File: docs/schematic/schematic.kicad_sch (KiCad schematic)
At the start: 9 parts, among them J1 AudioJack2, SW1 SW_Push, SW2 SW_Push, SW3 SW_Push, SW4 SW_Push

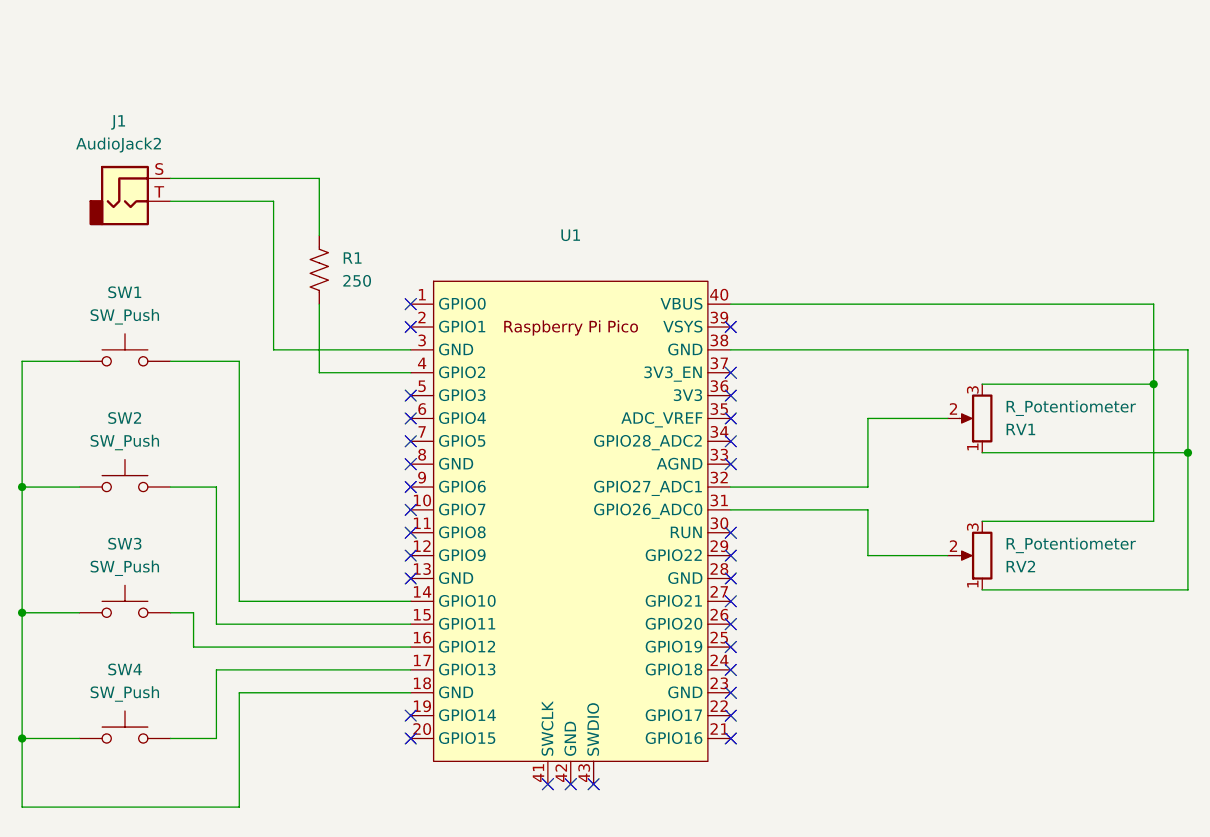
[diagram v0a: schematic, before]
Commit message: Update Schematic to as built
We deviated from the original schematic as it was simpler to construct/ source in the way we built  it.
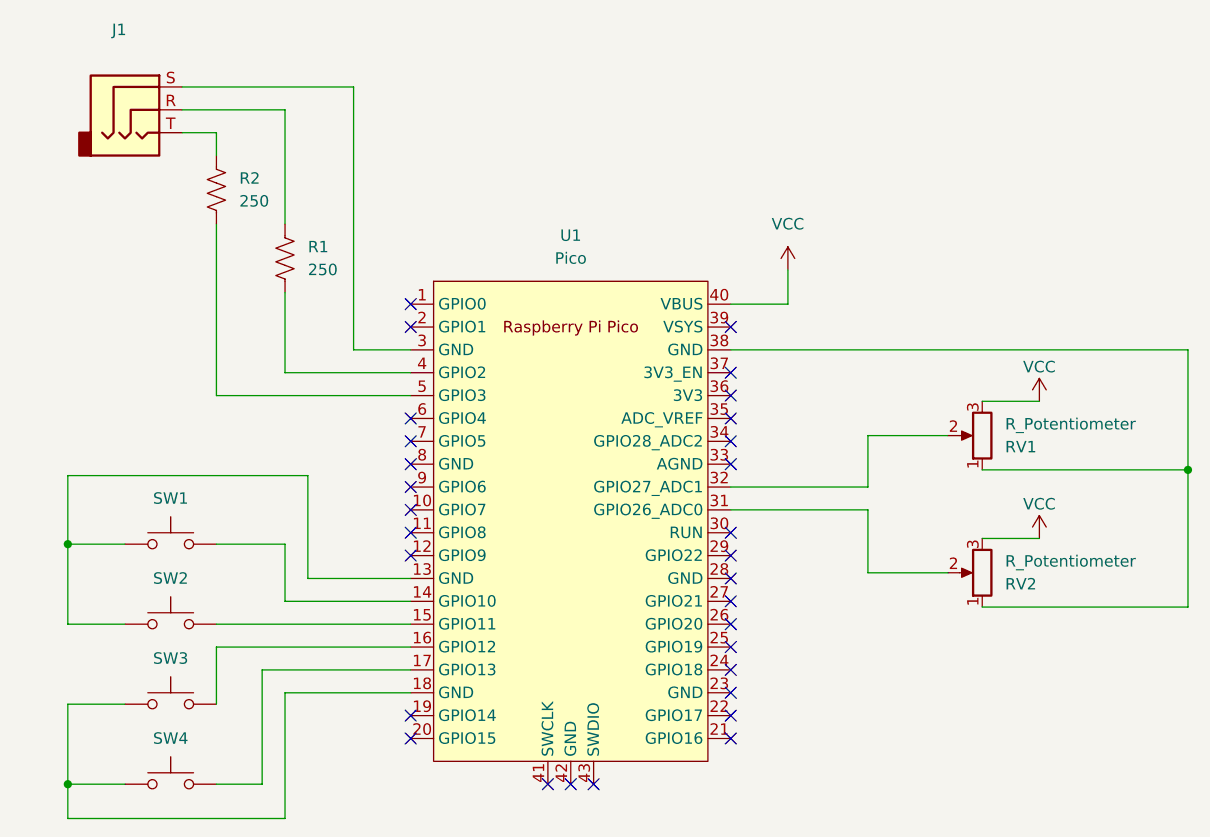
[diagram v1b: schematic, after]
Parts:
- removed J1: AudioJack2, Connector_Wire:SolderWire-0.15sqmm_1x02_P4mm_D0.5mm_OD1.5mm, symbol Connector:AudioJack2
- added J1: (no value), symbol Connector:AudioJack3
- added R2: 250, Resistor_THT:R_Axial_DIN0309_L9.0mm_D3.2mm_P15.24mm_Horizontal, symbol Device:R_US
- U1: value (none) -> Pico; footprint (none) -> MCU_RaspberryPi_and_Boards:RPi_Pico_SMD_TH
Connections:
- net at SW3.1, SW4.1, U1.18 (GND): no longer SW1.1, SW2.1
- net at R1.1: now also J1.R
- net VCC: now reaches RV1.3, RV2.3, U1.40 (VBUS)
- net at U1.3 (GND): now also J1.S
- net at U1.13 (GND): now also SW1.1, SW2.1
- net at U1.5 (GPIO3): now also R2.2
- new net: J1.T, R2.1
- no-connect marks 32 -> 30
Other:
- moved on the sheet: R1, RV1, RV2, SW2, SW3, SW4

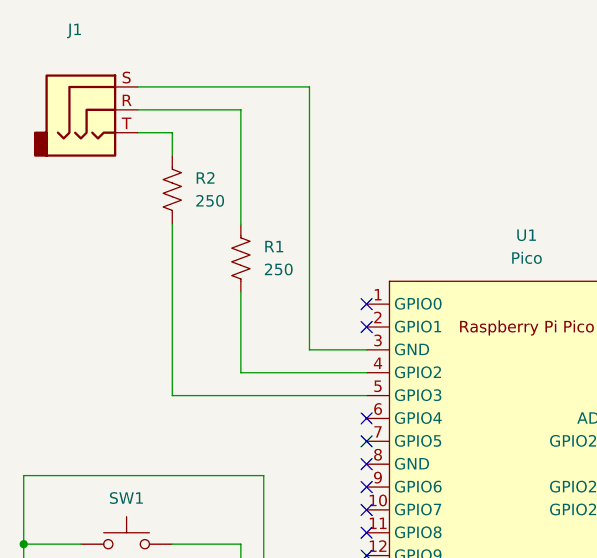
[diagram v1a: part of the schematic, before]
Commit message: Update Schematic
We found that the tone() function can only service one pin at a time, and that we can tie the t and r of the audio output together with no ill effects.
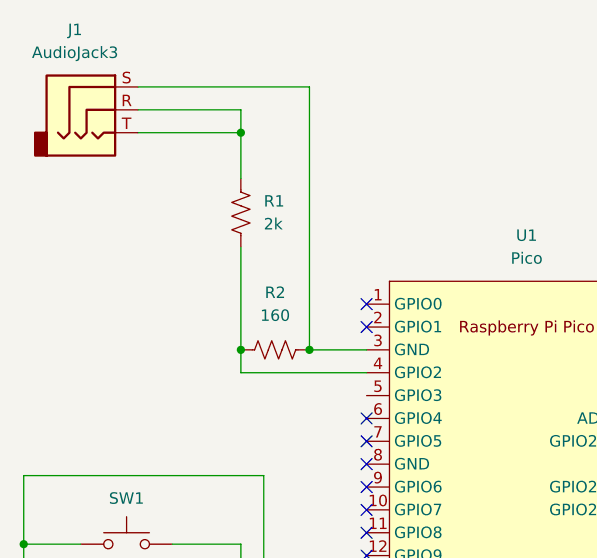
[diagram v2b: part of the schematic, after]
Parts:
- J1: value (none) -> AudioJack3; footprint (none) -> Connector_Audio:Jack_6.35mm_Neutrik_NJ3FD-V_Vertical
- R1: value 250 -> 2k
- R2: value 250 -> 160
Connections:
- net at J1.T: now also J1.R, R1.1; no longer R2.1
- net at R2.2: now also J1.S, U1.3 (GND); no longer U1.5 (GPIO3)
- net at R1.2, U1.4 (GPIO2): now also R2.1
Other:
- moved on the sheet: R1
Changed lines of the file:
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@@
     (rev "1.1")
   )
+  (junction (at 88.9 43.18) (diameter 0) (color 0 0 0 0)
+  )
   (junction (at 64.77 115.57) (diameter 0) (color 0 0 0 0)
+  )
+  (junction (at 96.52 67.31) (diameter 0) (color 0 0 0 0)
+  )
+  (junction (at 88.9 67.31) (diameter 0) (color 0 0 0 0)
   )
   (junction (at 189.23 80.645) (diameter 0) (color 0 0 0 0)
@@
     (stroke (width 0) (type default) (color 0 0 0 0))
   )
-  (wire (pts (xy 77.47 43.18) (xy 81.28 43.18))
-    (stroke (width 0) (type default) (color 0 0 0 0))
-  )
   (wire (pts (xy 88.9 95.25) (xy 102.87 95.25))
     (stroke (width 0) (type default) (color 0 0 0 0))
   )
+  (wire (pts (xy 88.9 67.31) (xy 88.9 69.85))
+    (stroke (width 0) (type default) (color 0 0 0 0))
+  )
   (wire (pts (xy 91.44 81.28) (xy 64.77 81.28))
     (stroke (width 0) (type default) (color 0 0 0 0))
@@
     (stroke (width 0) (type default) (color 0 0 0 0))
   )
-  (wire (pts (xy 81.28 43.18) (xy 81.28 45.72))
-    (stroke (width 0) (type default) (color 0 0 0 0))
-  )
   (wire (pts (xy 138.43 62.23) (xy 144.78 62.23))
     (stroke (width 0) (type default) (color 0 0 0 0))
@@
     (stroke (width 0) (type default) (color 0 0 0 0))
   )
-  (wire (pts (xy 96.52 67.31) (xy 96.52 38.1))
-    (stroke (width 0) (type default) (color 0 0 0 0))
-  )
   (wire (pts (xy 189.23 80.645) (xy 189.23 95.885))
     (stroke (width 0) (type default) (color 0 0 0 0))
@@
     (stroke (width 0) (type default) (color 0 0 0 0))
   )
+  (wire (pts (xy 77.47 43.18) (xy 88.9 43.18))
+    (stroke (width 0) (type default) (color 0 0 0 0))
+  )
   (wire (pts (xy 96.52 38.1) (xy 77.47 38.1))
     (stroke (width 0) (type default) (color 0 0 0 0))
@@
     (stroke (width 0) (type default) (color 0 0 0 0))
   )
-  (wire (pts (xy 88.9 40.64) (xy 88.9 53.34))
+  (wire (pts (xy 88.9 40.64) (xy 88.9 43.18))
     (stroke (width 0) (type default) (color 0 0 0 0))
   )
@@
     (stroke (width 0) (type default) (color 0 0 0 0))
   )
-  (wire (pts (xy 88.9 69.85) (xy 88.9 60.96))
+  (wire (pts (xy 88.9 43.18) (xy 88.9 48.26))
+    (stroke (width 0) (type default) (color 0 0 0 0))
+  )
+  (wire (pts (xy 88.9 55.88) (xy 88.9 67.31))
     (stroke (width 0) (type default) (color 0 0 0 0))
   )
@@
     (stroke (width 0) (type default) (color 0 0 0 0))
   )
+  (wire (pts (xy 96.52 38.1) (xy 96.52 67.31))
+    (stroke (width 0) (type default) (color 0 0 0 0))
+  )
   (wire (pts (xy 102.87 92.71) (xy 91.44 92.71))
     (stroke (width 0) (type default) (color 0 0 0 0))
   )
-  (wire (pts (xy 81.28 53.34) (xy 81.28 72.39))
-    (stroke (width 0) (type default) (color 0 0 0 0))
-  )
   (wire (pts (xy 166.37 73.025) (xy 172.72 73.025))
     (stroke (width 0) (type default) (color 0 0 0 0))
@@
     (stroke (width 0) (type default) (color 0 0 0 0))
   )
-  (wire (pts (xy 102.87 72.39) (xy 81.28 72.39))
-    (stroke (width 0) (type default) (color 0 0 0 0))
-  )
   (wire (pts (xy 153.67 82.55) (xy 138.43 82.55))
     (stroke (width 0) (type default) (color 0 0 0 0))
@@
   (wire (pts (xy 102.87 100.33) (xy 81.28 100.33))
     (stroke (width 0) (type default) (color 0 0 0 0))
-  )
-  (symbol (lib_id "Device:R_US") (at 81.28 49.53 0) (unit 1)
-    (in_bom yes) (on_board yes) (fields_autoplaced)
-    (property "Reference" "R2" (id 0) (at 83.82 48.2599 0)
-      (effects (font (size 1.27 1.27)) (justify left))
-    )
-    (property "Value" "250" (id 1) (at 83.82 50.7999 0)
-      (effects (font (size 1.27 1.27)) (justify left))
-    )
-    (property "Footprint" "Resistor_THT:R_Axial_DIN0309_L9.0mm_D3.2mm_P15.24mm_Horizontal" (id 2) (at 82.296 49.784 90)
-      (effects (font (size 1.27 1.27)) hide)
-    )
-    (property "Datasheet" "~" (id 3) (at 81.28 49.53 0)
-      (effects (font (size 1.27 1.27)) hide)
-    )
-    (property "Spice_Primitive" "R" (id 4) (at 81.28 49.53 0)
-      (effects (font (size 1.27 1.27)) hide)
-    )
-    (property "Spice_Model" "250" (id 5) (at 81.28 49.53 0)
-      (effects (font (size 1.27 1.27)) hide)
-    )
-    (property "Spice_Netlist_Enabled" "Y" (id 6) (at 81.28 49.53 0)
-      (effects (font (size 1.27 1.27)) hide)
-    )
-    (pin "1")
-    (pin "2")
   )
   (symbol (lib_id "power:VCC") (at 172.72 88.265 0) (unit 1)
@@
     (pin "2")
   )
-  (symbol (lib_id "Device:R_US") (at 88.9 57.15 0) (unit 1)
-    (in_bom yes) (on_board yes) (fields_autoplaced)
-    (property "Reference" "R1" (id 0) (at 91.44 55.8799 0)
+  (symbol (lib_id "Device:R_US") (at 88.9 52.07 0) (unit 1)
+    (in_bom yes) (on_board yes) (fields_autoplaced)
+    (property "Reference" "R1" (id 0) (at 91.44 50.7999 0)
       (effects (font (size 1.27 1.27)) (justify left))
     )
-    (property "Value" "250" (id 1) (at 91.44 58.4199 0)
+    (property "Value" "2k" (id 1) (at 91.44 53.3399 0)
       (effects (font (size 1.27 1.27)) (justify left))
     )
-    (property "Footprint" "Resistor_THT:R_Axial_DIN0309_L9.0mm_D3.2mm_P15.24mm_Horizontal" (id 2) (at 89.916 57.404 90)
-      (effects (font (size 1.27 1.27)) hide)
-    )
-    (property "Datasheet" "~" (id 3) (at 88.9 57.15 0)
-      (effects (font (size 1.27 1.27)) hide)
-    )
-    (property "Spice_Primitive" "R" (id 4) (at 88.9 57.15 0)
-      (effects (font (size 1.27 1.27)) hide)
-    )
-    (property "Spice_Model" "250" (id 5) (at 88.9 57.15 0)
-      (effects (font (size 1.27 1.27)) hide)
-    )
-    (property "Spice_Netlist_Enabled" "Y" (id 6) (at 88.9 57.15 0)
+    (property "Footprint" "Resistor_THT:R_Axial_DIN0309_L9.0mm_D3.2mm_P15.24mm_Horizontal" (id 2) (at 89.916 52.324 90)
+      (effects (font (size 1.27 1.27)) hide)
+    )
+    (property "Datasheet" "~" (id 3) (at 88.9 52.07 0)
+      (effects (font (size 1.27 1.27)) hide)
+    )
+    (property "Spice_Primitive" "R" (id 4) (at 88.9 52.07 0)
+      (effects (font (size 1.27 1.27)) hide)
+    )
+    (property "Spice_Model" "250" (id 5) (at 88.9 52.07 0)
+      (effects (font (size 1.27 1.27)) hide)
+    )
+    (property "Spice_Netlist_Enabled" "Y" (id 6) (at 88.9 52.07 0)
       (effects (font (size 1.27 1.27)) hide)
     )
@@
     )
     (property "Datasheet" "~" (id 3) (at 76.2 92.71 0)
+      (effects (font (size 1.27 1.27)) hide)
+    )
+    (pin "1")
+    (pin "2")
+  )
+  (symbol (lib_id "Device:R_US") (at 92.71 67.31 90) (unit 1)
+    (in_bom yes) (on_board yes) (fields_autoplaced)
+    (property "Reference" "R2" (id 0) (at 92.71 60.96 90))
+    (property "Value" "160" (id 1) (at 92.71 63.5 90))
+    (property "Footprint" "Resistor_THT:R_Axial_DIN0309_L9.0mm_D3.2mm_P15.24mm_Horizontal" (id 2) (at 92.964 66.294 90)
+      (effects (font (size 1.27 1.27)) hide)
+    )
+    (property "Datasheet" "~" (id 3) (at 92.71 67.31 0)
+      (effects (font (size 1.27 1.27)) hide)
+    )
+    (property "Spice_Primitive" "R" (id 4) (at 92.71 67.31 0)
+      (effects (font (size 1.27 1.27)) hide)
+    )
+    (property "Spice_Model" "250" (id 5) (at 92.71 67.31 0)
+      (effects (font (size 1.27 1.27)) hide)
+    )
+    (property "Spice_Netlist_Enabled" "Y" (id 6) (at 92.71 67.31 0)
       (effects (font (size 1.27 1.27)) hide)
     )
@@
     (in_bom yes) (on_board yes) (fields_autoplaced)
     (property "Reference" "J1" (id 0) (at 70.485 31.75 0))
-    (property "Value" "" (id 1) (at 70.485 34.29 0))
-    (property "Footprint" "" (id 2) (at 72.39 40.64 0)
+    (property "Value" "AudioJack3" (id 1) (at 70.485 34.29 0))
+    (property "Footprint" "Connector_Audio:Jack_6.35mm_Neutrik_NJ3FD-V_Vertical" (id 2) (at 72.39 40.64 0)
       (effects (font (size 1.27 1.27)) hide)
     )
@@
     )
     (path "/389ab245-da99-49ed-8639-e5829257346a"
-      (reference "R1") (unit 1) (value "250") (footprint "Resistor_THT:R_Axial_DIN0309_L9.0mm_D3.2mm_P15.24mm_Horizontal")
-    )
-    (path "/00661feb-5425-4dda-89e1-c22739bec574"
-      (reference "R2") (unit 1) (value "250") (footprint "Resistor_THT:R_Axial_DIN0309_L9.0mm_D3.2mm_P15.24mm_Horizontal")
+      (reference "R1") (unit 1) (value "2k") (footprint "Resistor_THT:R_Axial_DIN0309_L9.0mm_D3.2mm_P15.24mm_Horizontal")
+    )
+    (path "/5d708b1d-f53e-4c26-a11a-dd207e069a6f"
+      (reference "R2") (unit 1) (value "160") (footprint "Resistor_THT:R_Axial_DIN0309_L9.0mm_D3.2mm_P15.24mm_Horizontal")
     )
     (path "/ae2d847c-72ca-4d0f-acb3-ead936959a93"
